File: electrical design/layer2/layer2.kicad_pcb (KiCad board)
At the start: 2 copper layers, 178 x 168.1 mm, 36 parts, among them J1 Conn_01x01_Female, J10 Conn_01x01_Female, J2 Conn_01x01_Female, J3 Conn_01x01_Female, J4 Conn_01x01_Female, J5 Conn_01x01_Female, J6 Conn_01x01_Female, J7 Conn_01x01_Female, J8 Conn_01x01_Female, J9 Conn_01x01_Female

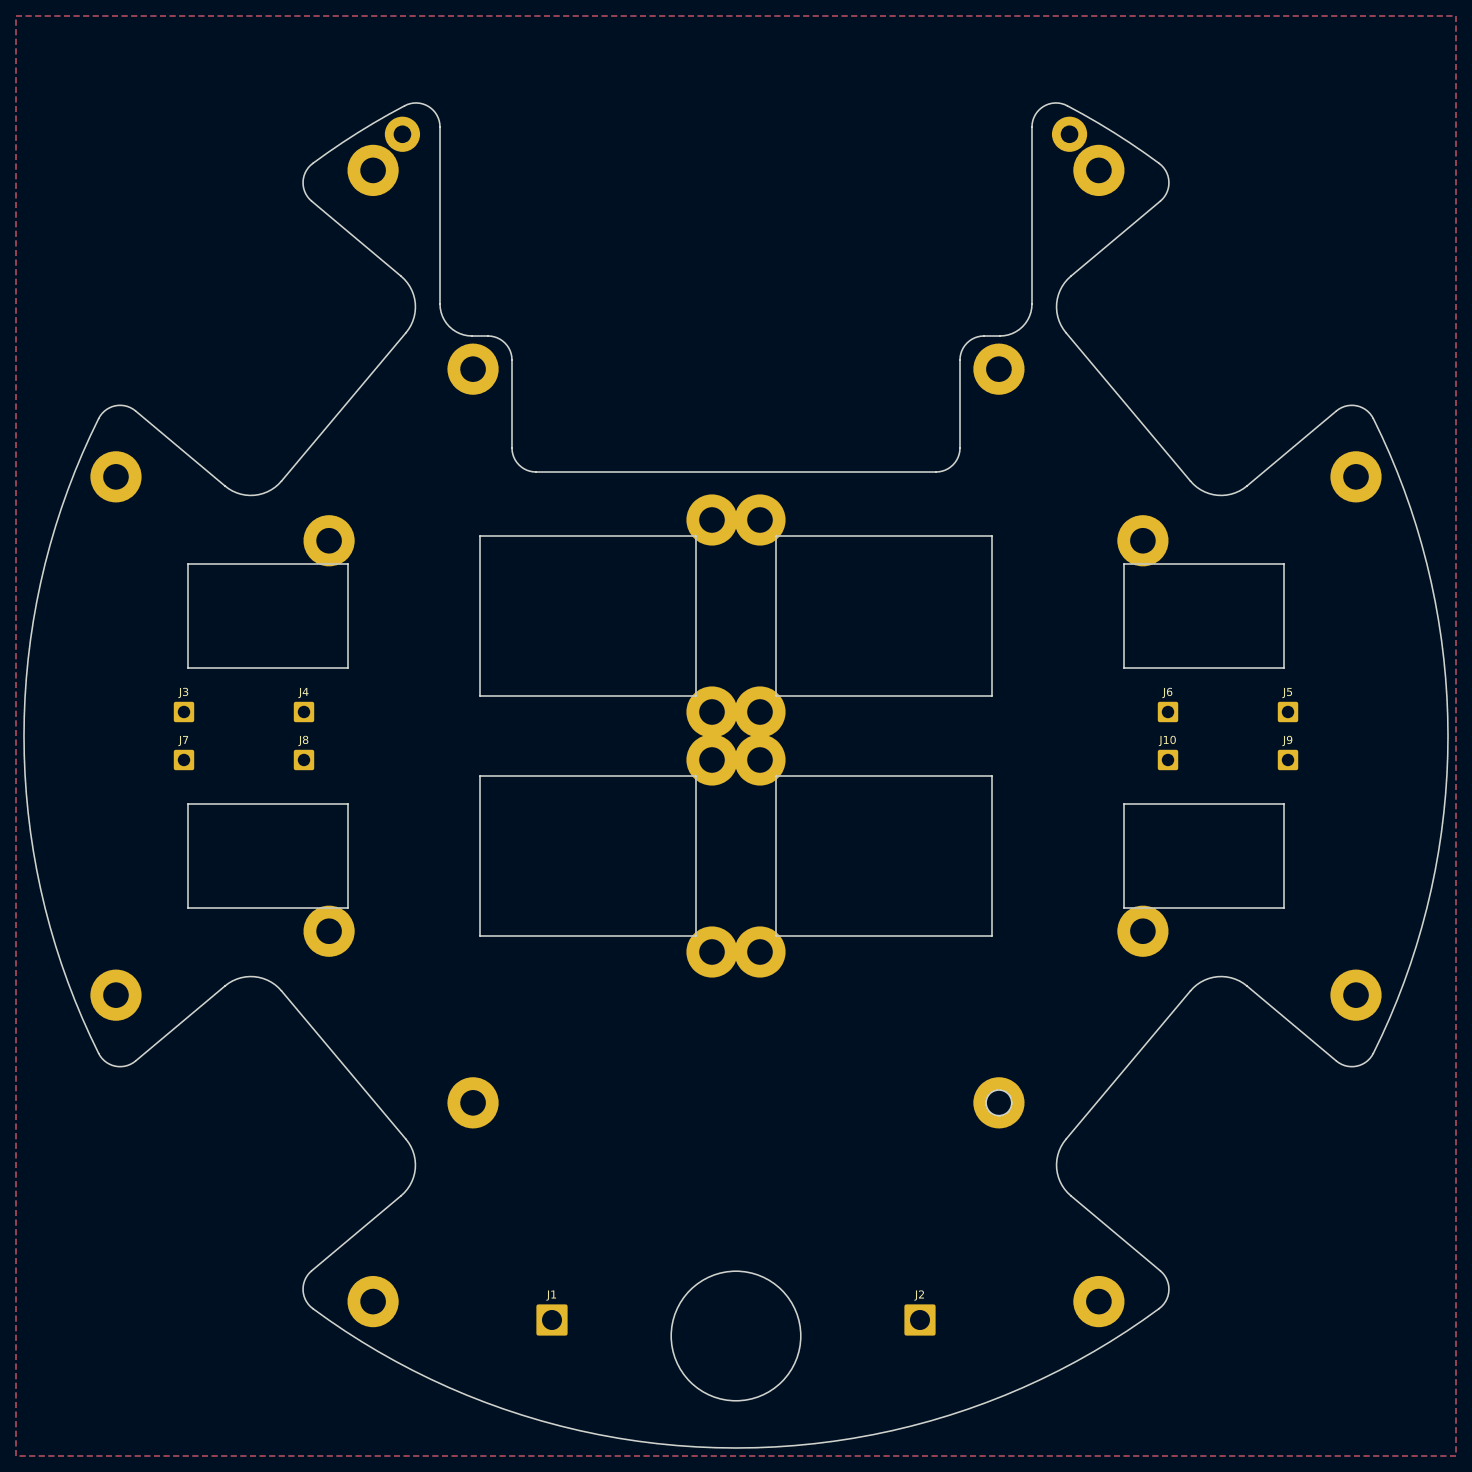
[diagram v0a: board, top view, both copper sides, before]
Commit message: add connectors for power transfer to l3
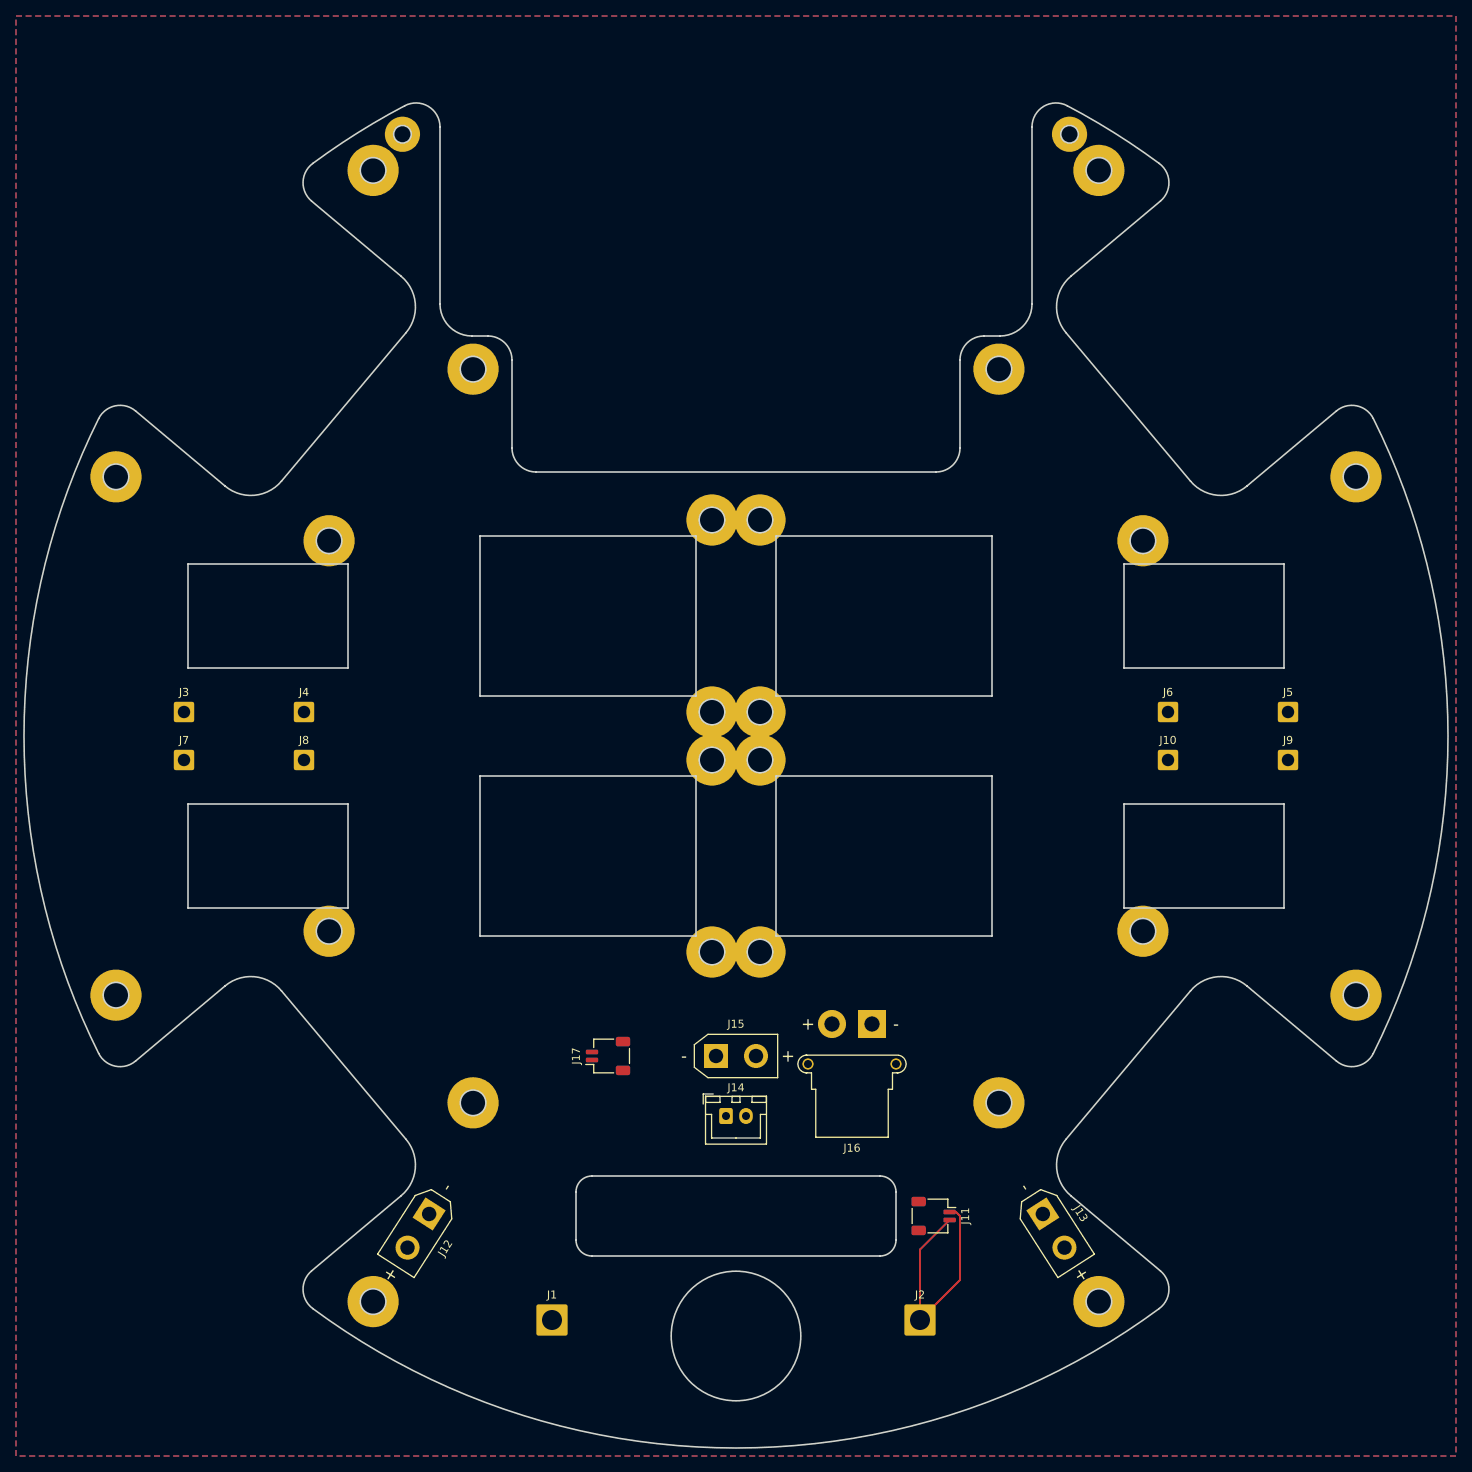
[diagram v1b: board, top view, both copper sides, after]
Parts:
- added J11: SH1.0 2P, Connector_JST:JST_SH_SM02B-SRSS-TB_1x02-1MP_P1.00mm_Horizontal, F.Cu at (129.7, 165.0)
- added J12: XT60-F, Connector_AMASS:AMASS_XT30UPB-F_1x02_P5.0mm_Vertical, F.Cu at (66.6, 164.7)
- added J13: XT60-F, Connector_AMASS:AMASS_XT30UPB-F_1x02_P5.0mm_Vertical, F.Cu at (143.4, 164.7)
- added J14: XH2.54 2P, Connector_JST:JST_XH_B2B-XH-A_1x02_P2.50mm_Vertical, F.Cu at (103.8, 152.5)
- added J15: XT60-F, Connector_AMASS:AMASS_XT30UPB-F_1x02_P5.0mm_Vertical, F.Cu at (102.5, 145.0)
- added J16: XT60-F, Connector_AMASS:AMASS_XT30PW-F_1x02_P2.50mm_Horizontal, F.Cu at (122.0, 141.0)
- added J17: SH1.0 2P, Connector_JST:JST_SH_SM02B-SRSS-TB_1x02-1MP_P1.00mm_Horizontal, F.Cu at (89.0, 145.0)
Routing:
- net GND: track 0.00 -> 32.0 mm
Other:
- outline, holes or cut-outs redrawn

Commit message: update pcbs and mech drawings
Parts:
- J1, J2: footprint Connector_Wire:SolderWire-2sqmm_1x01_D2mm_OD3.9mm -> Connector_Wire:SolderWire-2.5sqmm_1x01_D2.4mm_OD4.4mm
- J10, J3, J4, J5, J6, J7, J8, J9: footprint Connector_Wire:SolderWire-0.75sqmm_1x01_D1.25mm_OD2.3mm -> Connector_Wire:SolderWire-2sqmm_1x01_D2mm_OD3.9mm
